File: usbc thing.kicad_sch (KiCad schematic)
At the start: 15 parts, among them J1 USB_C_Receptacle_USB2.0_16P, Q1 NMOS, U1 P26744EAATRHBRQ1, U4 TPD4S480RUKR

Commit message: changes after 2-26 work meeting
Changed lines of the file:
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@@
+	)
+	(junction
+		(at 40.64 40.64)
+		(diameter 0)
+		(color 0 0 0 0)
 	)
 	(junction
@@
 	)
 	(junction
-		(at 41.91 40.64)
-		(diameter 0)
-		(color 0 0 0 0)
-	)
-	(junction
 		(at 148.59 177.8)
 		(diameter 0)
@@
 	(wire
 		(pts
-			(xy 43.18 40.64) (xy 41.91 40.64)
+			(xy 33.02 40.64) (xy 40.64 40.64)
 		)
 		(stroke
@@
 	(wire
 		(pts
+			(xy 40.64 40.64) (xy 43.18 40.64)
+		)
+		(stroke
+			(width 0)
+			(type default)
+		)
+	)
+	(wire
+		(pts
 			(xy 24.13 73.66) (xy 33.02 73.66)
 		)
@@
 	(wire
 		(pts
-			(xy 41.91 39.37) (xy 41.91 40.64)
-		)
-		(stroke
-			(width 0)
-			(type default)
-		)
-	)
-	(wire
-		(pts
 			(xy 170.18 45.72) (xy 173.99 45.72)
 		)
@@
 	(wire
 		(pts
-			(xy 41.91 40.64) (xy 33.02 40.64)
-		)
-		(stroke
-			(width 0)
-			(type default)
-		)
-	)
-	(wire
-		(pts
-			(xy 41.91 39.37) (xy 45.72 39.37)
-		)
-		(stroke
-			(width 0)
-			(type default)
-		)
-	)
-	(wire
-		(pts
 			(xy 129.54 125.73) (xy 179.07 125.73)
 		)
@@
 	(wire
 		(pts
-			(xy 45.72 39.37) (xy 45.72 26.67)
+			(xy 40.64 26.67) (xy 40.64 40.64)
 		)
 		(stroke
@@
 	(label "SDA"
 		(at 38.1 68.58 0)
-		(effects
-			(font
-				(size 1.27 1.27)
-			)
-			(justify left bottom)
-		)
-	)
-	(label "Vin_40V"
-		(at 41.91 40.64 0)
 		(effects
 			(font
@@
 	(symbol
 		(lib_id "power:+5V")
-		(at 45.72 26.67 0)
+		(at 40.64 26.67 0)
 		(unit 1)
 		(exclude_from_sim no)
@@
 		(fields_autoplaced yes)
 		(property "Reference" "#PWR02"
-			(at 45.72 30.48 0)
+			(at 40.64 30.48 0)
 			(effects
 				(font
@@
 		)
 		(property "Value" "+5V"
-			(at 45.72 21.59 0)
+			(at 40.64 21.59 0)
 			(effects
 				(font
@@
 		)
 		(property "Footprint" ""
-			(at 45.72 26.67 0)
+			(at 40.64 26.67 0)
 			(effects
 				(font
@@
 		)
 		(property "Datasheet" ""
-			(at 45.72 26.67 0)
+			(at 40.64 26.67 0)
 			(effects
 				(font
@@
 		)
 		(property "Description" "Power symbol creates a global label with name \"+5V\""
-			(at 45.72 26.67 0)
-			(effects
-				(font
+			(at 40.64 26.67 0)
+			(effects
+				(font

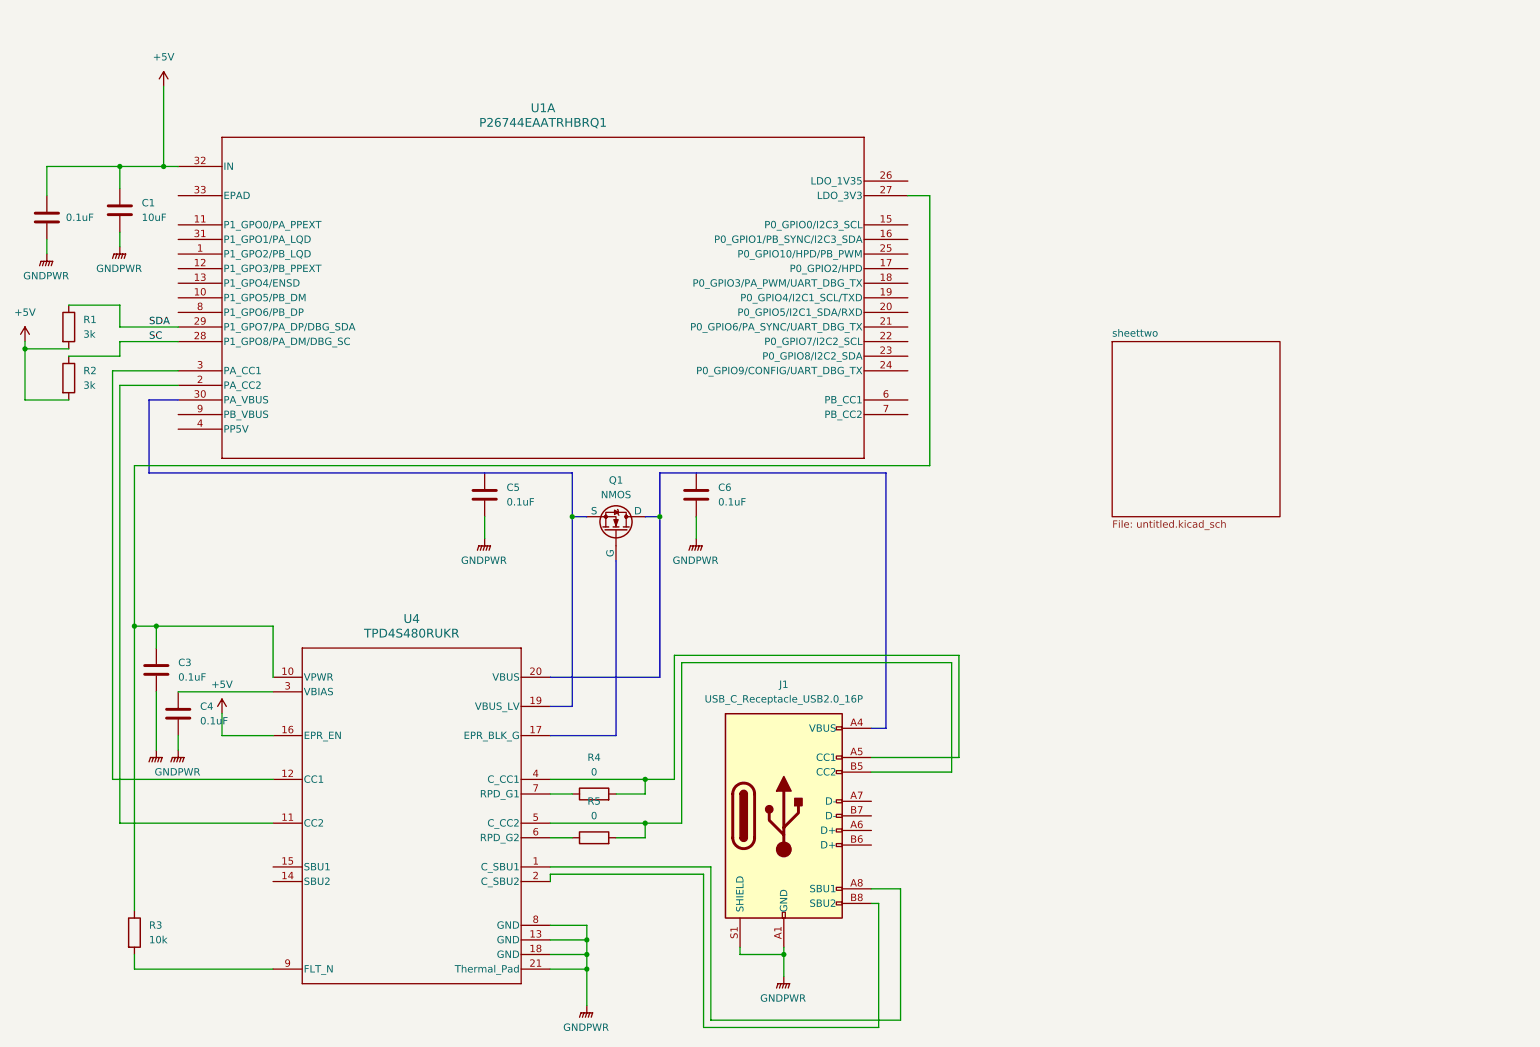
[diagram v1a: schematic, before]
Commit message: need to add buck converter for dc to pd controller
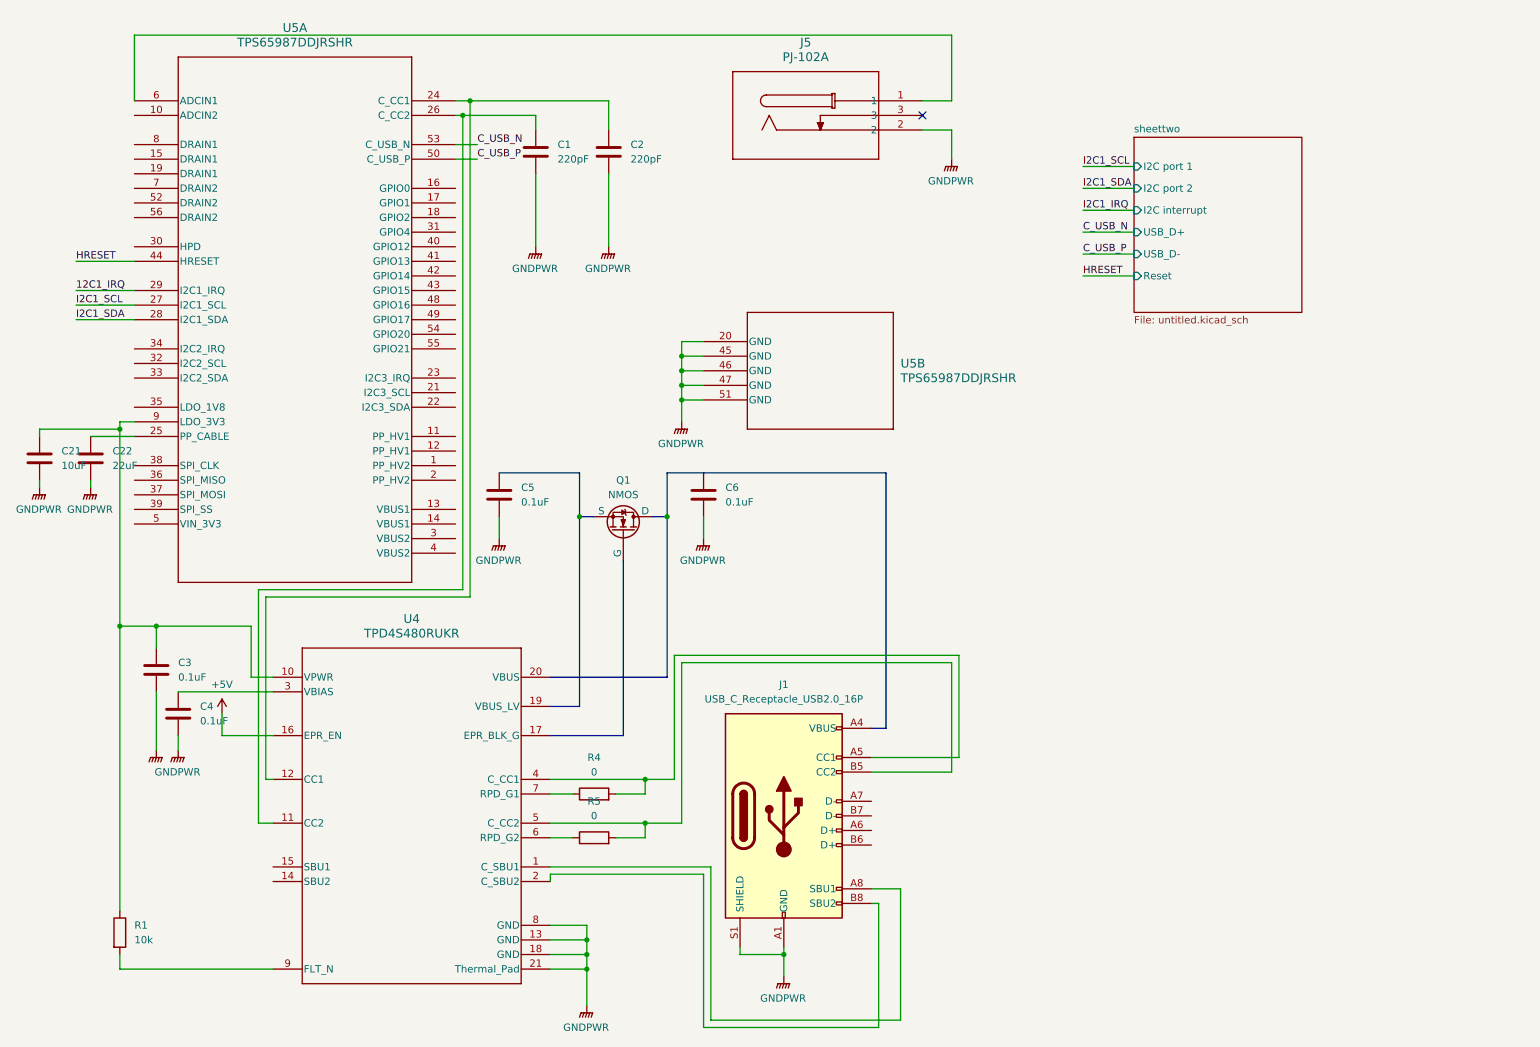
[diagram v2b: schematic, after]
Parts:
- removed R2: 3k, symbol Device:R
- removed R3: 10k, symbol Device:R
- removed U1: P26744EAATRHBRQ1, VQFN32_5P1X5P1_TEX, symbol TPS26744E-Q1:P26744EAATRHBRQ1
- added C21: 10uF, symbol Device:C
- added C22: 22uF, symbol Device:C
- added J5: PJ-102A, PJ-102A_CUD, symbol dc barrel thingy:PJ-102A
- added U5: TPS65987DDJRSHR, VQFN56_RSH0056E_7X7_TEX, symbol TPS65987DDJ:TPS65987DDJRSHR
- C1: value 10uF -> 220pF
- C2: value 0.1uF -> 220pF
- R1: value 3k -> 10k
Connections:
- net SDA is gone; now on an unnamed net: R1.1
- net +5V: no longer C1.1, C2.1, R1.2
- net GNDPWR: now also C21.2, C22.2, J5.2, U5.20 (GND), U5.45 (GND), U5.46 (GND), U5.47 (GND), U5.51 (GND)
- net at C3.1, U4.10 (VPWR): now also C21.1, U5.9 (LDO_3V3)
- net at U4.9 (FLT_N): now also R1.2
- net at U4.11 (CC2): now also C1.1, U5.26 (C_CC2)
- net at U4.12 (CC1): now also C2.1, U5.24 (C_CC1)
- new net: J5.1, U5.6 (ADCIN1)
- new net: C22.1, U5.25 (PP_CABLE)
- new net 12C1_IRQ: U5.29 (I2C1_IRQ)
- new net C_USB_N: U5.53 (C_USB_N)
- new net C_USB_P: U5.50 (C_USB_P)
- new net HRESET: U5.44 (HRESET)
- new net I2C1_SCL: U5.27 (I2C1_SCL)
- new net I2C1_SDA: U5.28 (I2C1_SDA)
- no-connect marks 0 -> 1
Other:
- sheet sheettwo ports: added I2C interrupt, I2C port 1, I2C port 2, Reset, USB_D+, USB_D-; removed none
- moved on the sheet: C5, C6, Q1

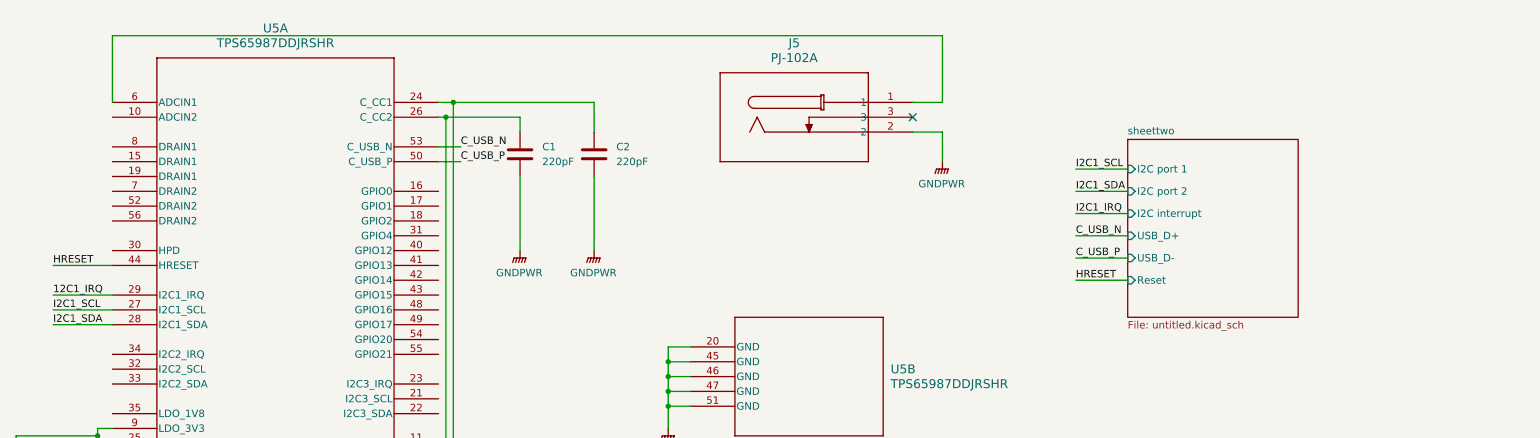
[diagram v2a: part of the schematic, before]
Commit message: added buck diagram
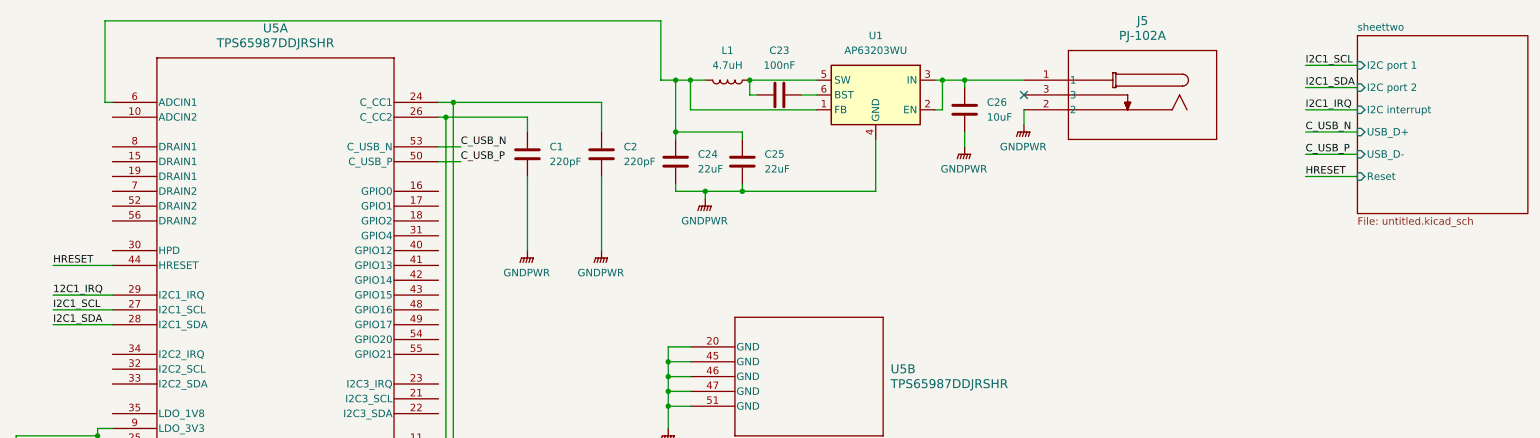
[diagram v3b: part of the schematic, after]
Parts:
- added C23: 100nF, symbol Device:C
- added C24, C25: 22uF, symbol Device:C
- added C26: 10uF, symbol Device:C
- added L1: 4.7uH, symbol Device:L
- added U1: AP63203WU, Package_TO_SOT_SMD:TSOT-23-6, symbol Regulator_Switching:AP63203WU
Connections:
- net GNDPWR: now also C24.2, C25.2, C26.2, U1.4 (GND)
- net at U5.6 (ADCIN1): now also C24.1, C25.1, L1.2, U1.1 (FB); no longer J5.1
- new net: C26.1, J5.1, U1.2 (EN), U1.3 (IN)
- new net: C23.1, L1.1, U1.5 (SW)
- new net: C23.2, U1.6 (BST)
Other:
- moved on the sheet: C1, C2, J5

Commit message: added footprints
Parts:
- C1, C2, C21, C22, C23, C24, C25, C26, C3, C4, C5, C6: footprint (none) -> Capacitor_SMD:C_1206_3216Metric
- J1: footprint (none) -> Library:GCT_USB4216-03-A_REVA
- J5: footprint PJ-102A_CUD -> Connector_BarrelJack:BarrelJack_CUI_PJ-102AH_Horizontal
- L1: footprint (none) -> Inductor_SMD:L_Sunlord_MWSA1206S-4R7
- Q1: footprint (none) -> Package_TO_SOT_THT:TO-3P-3_Horizontal_TabDown
- R1, R4, R5: footprint (none) -> Resistor_SMD:R_1206_3216Metric
- U4: footprint RUK0020B-IPC_A -> Library:RUK0020B-IPC_A
- U5: footprint VQFN56_RSH0056E_7X7_TEX -> Library:VQFN56_RSH0056E_7X7_TEX
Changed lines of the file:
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@@
 			)
 		)
-		(property "Footprint" ""
+		(property "Footprint" "Capacitor_SMD:C_1206_3216Metric"
 			(at 144.4752 43.18 0)
 			(effects
@@
 			)
 		)
-		(property "Footprint" "PJ-102A_CUD"
+		(property "Footprint" "Connector_BarrelJack:BarrelJack_CUI_PJ-102AH_Horizontal"
 			(at 191.77 25.4 0)
 			(effects
@@
 			)
 		)
-		(property "Footprint" ""
+		(property "Footprint" "Library:GCT_USB4216-03-A_REVA"
 			(at 152.4 153.67 0)
 			(effects
@@
 			)
 		)
-		(property "Footprint" ""
+		(property "Footprint" "Capacitor_SMD:C_1206_3216Metric"
 			(at 100.0252 101.6 0)
 			(effects
@@
 			)
 		)
-		(property "Footprint" ""
+		(property "Footprint" "Capacitor_SMD:C_1206_3216Metric"
 			(at 153.67 26.9748 0)
 			(effects
@@
 			)
 		)
-		(property "Footprint" ""
+		(property "Footprint" "Inductor_SMD:L_Sunlord_MWSA1206S-4R7"
 			(at 140.97 25.4 0)
 			(effects
@@
 			)
 		)
-		(property "Footprint" ""
+		(property "Footprint" "Resistor_SMD:R_1206_3216Metric"
 			(at 115.57 151.638 90)
 			(effects
@@
 			)
 		)
-		(property "Footprint" "VQFN56_RSH0056E_7X7_TEX"
+		(property "Footprint" "Library:VQFN56_RSH0056E_7X7_TEX"
 			(at 35.56 29.21 0)
 			(effects
@@
 			)
 		)
-		(property "Footprint" ""
+		(property "Footprint" "Resistor_SMD:R_1206_3216Metric"
 			(at 115.57 159.258 90)
 			(effects
@@
 			)
 		)
-		(property "Footprint" "VQFN56_RSH0056E_7X7_TEX"
+		(property "Footprint" "Library:VQFN56_RSH0056E_7X7_TEX"
 			(at 134.62 71.12 0)
 			(effects
@@
 			)
 		)
-		(property "Footprint" ""
+		(property "Footprint" "Capacitor_SMD:C_1206_3216Metric"
 			(at 44.1452 139.7 0)
 			(effects
@@
 			)
 		)
-		(property "Footprint" ""
+		(property "Footprint" "Capacitor_SMD:C_1206_3216Metric"
 			(at 28.9052 95.25 0)
 			(effects
@@
 			)
 		)
-		(property "Footprint" ""
+		(property "Footprint" "Capacitor_SMD:C_1206_3216Metric"
 			(at 20.0152 95.25 0)
 			(effects
@@
 			)
 		)
-		(property "Footprint" ""
+		(property "Footprint" "Package_TO_SOT_THT:TO-3P-3_Horizontal_TabDown"
 			(at 123.19 99.06 0)
 			(effects
@@
 			)
 		)
-		(property "Footprint" ""
+		(property "Footprint" "Capacitor_SMD:C_1206_3216Metric"
 			(at 40.3352 132.08 0)
 			(effects
@@
 			)
 		)
-		(property "Footprint" ""
+		(property "Footprint" "Capacitor_SMD:C_1206_3216Metric"
 			(at 135.5852 101.6 0)
 			(effects
@@
 			)
 		)
-		(property "Footprint" ""
+		(property "Footprint" "Capacitor_SMD:C_1206_3216Metric"
 			(at 107.6452 41.91 0)
 			(effects
@@
 			)
 		)
-		(property "Footprint" "RUK0020B-IPC_A"
+		(property "Footprint" "Library:RUK0020B-IPC_A"
 			(at 59.69 129.54 0)
 			(effects
@@
 			)
 		)
-		(property "Footprint" ""
+		(property "Footprint" "Resistor_SMD:R_1206_3216Metric"
 			(at 31.242 173.99 90)
 			(effects
@@
 			)
 		)
-		(property "Footprint" ""
+		(property "Footprint" "Capacitor_SMD:C_1206_3216Metric"
 			(at 120.3452 41.91 0)
 			(effects
@@
 			)
 		)
-		(property "Footprint" ""
+		(property "Footprint" "Capacitor_SMD:C_1206_3216Metric"
 			(at 182.5752 34.29 0)
 			(effects
@@
 			)
 		)
-		(property "Footprint" ""
+		(property "Footprint" "Capacitor_SMD:C_1206_3216Metric"
 			(at 133.0452 43.18 0)
 			(effects
